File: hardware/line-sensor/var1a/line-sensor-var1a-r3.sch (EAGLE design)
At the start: 142 parts, among them IC1 GP2S60, IC10 GP2S60, IC11 GP2S60, IC12 GP2S60, IC13 GP2S60, IC14 GP2S60, IC15 GP2S60, IC16 GP2S60, IC17 GP2S60, IC18 GP2S60, IC19 GP2S60, IC2 GP2S60, IC20 GP2S60, IC21 GP2S60, IC22 GP2S60, IC23 GP2S60, IC24 GP2S60, IC25 GP2S60, IC26 GP2S60, IC27 GP2S60, IC28 STM32L151VE, IC3 GP2S60, IC32 LM5165YDRCR, IC4 GP2S60, IC5 GP2S60, IC6 GP2S60, IC7 GP2S60, IC8 GP2S60, IC9 GP2S60, J1 MOLEX-502382-06XX, J2 MOLEX-53261-0771, J3 MOLEX-502382-03XX, Y1 CRYSTALKYOCERA-CX3225GB24000D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, Y2 CRYSTALNDK-NX3215SA

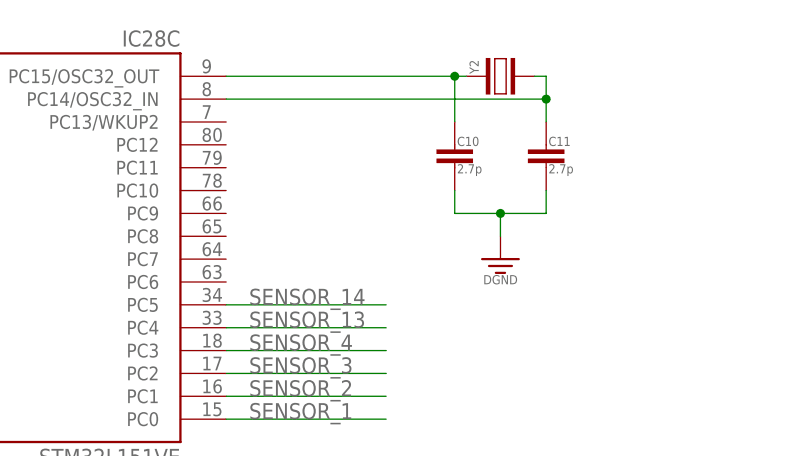
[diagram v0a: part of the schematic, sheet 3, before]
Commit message: - watchdog will now reset if either ADC or SPI didn't report in
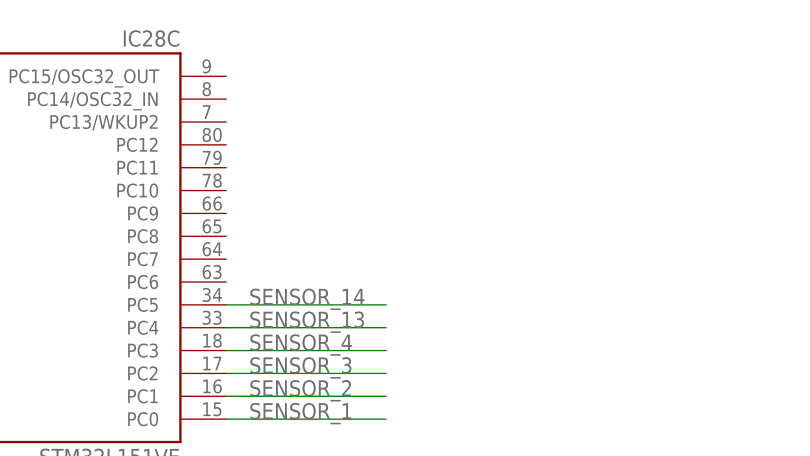
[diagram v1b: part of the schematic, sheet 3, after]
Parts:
- removed C10, C11: 2.7p, passives:CAPACITOR0402
- removed Y2: CRYSTALNDK-NX3215SA, passives:CRYSTALNDK-NX3215SA
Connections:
- removed net N$36: C10.1, IC28C.PC15/OSC32_OUT, Y2.1
- removed net N$37: C11.1, IC28C.PC14/OSC32_IN, Y2.2
- net GND: no longer C10.2, C11.2
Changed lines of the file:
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@@
 <part name="R67" library="passives" library_urn="urn:adsk.eagle:library:9287022" deviceset="RESISTOR" device="0603" package3d_urn="urn:adsk.eagle:package:704947/4" value="121k 1%"/>
 <part name="GND12" library="voltage-ground" library_urn="urn:adsk.eagle:library:704746" deviceset="GND" device=""/>
-<part name="L1" library="passives" library_urn="urn:adsk.eagle:library:9287022" deviceset="INDUCTOR" device="PANASONIC-SERIES-H" package3d_urn="urn:adsk.eagle:package:9314563/2" value="150u 0.86R 0.35A"/>
+<part name="L1" library="passives" library_urn="urn:adsk.eagle:library:9287022" deviceset="INDUCTOR" device="PANASONIC-SERIES-H" package3d_urn="urn:adsk.eagle:package:9314563/3" value="150u 0.86R 0.35A"/>
 <part name="C19" library="passives" library_urn="urn:adsk.eagle:library:9287022" deviceset="CAPACITOR" device="0603" package3d_urn="urn:adsk.eagle:package:704999/4" value="33n 10V X7R"/>
 <part name="DGND12" library="voltage-ground" library_urn="urn:adsk.eagle:library:704746" deviceset="DGND" device=""/>
 <part name="DGND13" library="voltage-ground" library_urn="urn:adsk.eagle:library:704746" deviceset="DGND" device=""/>
 <part name="R68" library="passives" library_urn="urn:adsk.eagle:library:9287022" deviceset="RESISTOR" device="0603" package3d_urn="urn:adsk.eagle:package:704947/4" value="0.5 5%"/>
-<part name="C20" library="passives" library_urn="urn:adsk.eagle:library:9287022" deviceset="CAPACITOR" device="0805" package3d_urn="urn:adsk.eagle:package:704997/4" value="22u 10V X7S"/>
+<part name="C20" library="passives" library_urn="urn:adsk.eagle:library:9287022" deviceset="CAPACITOR" device="0805" package3d_urn="urn:adsk.eagle:package:704997/5" value="22u 10V X7S"/>
 <part name="DGND14" library="voltage-ground" library_urn="urn:adsk.eagle:library:704746" deviceset="DGND" device=""/>
 <part name="SUPPLY37" library="voltage-ground" library_urn="urn:adsk.eagle:library:704746" deviceset="+3.3V" device=""/>
 <part name="FRAME5" library="frames" library_urn="urn:adsk.eagle:library:229" deviceset="A4L-LOC" device=""/>
-<part name="Y1" library="passives" library_urn="urn:adsk.eagle:library:9287022" deviceset="CRYSTAL" device="KYOCERA-CX3225GB24000D0HEQ" package3d_urn="urn:adsk.eagle:package:9990572/4"/>
+<part name="Y1" library="passives" library_urn="urn:adsk.eagle:library:9287022" deviceset="CRYSTAL" device="KYOCERA-CX3225GB24000D0HEQ" package3d_urn="urn:adsk.eagle:package:9990572/5"/>
 <part name="C8" library="passives" library_urn="urn:adsk.eagle:library:9287022" deviceset="CAPACITOR" device="0402" package3d_urn="urn:adsk.eagle:package:11874712/3" value="4.3p"/>
 <part name="C9" library="passives" library_urn="urn:adsk.eagle:library:9287022" deviceset="CAPACITOR" device="0402" package3d_urn="urn:adsk.eagle:package:11874712/3" value="4.3p"/>
 <part name="DGND15" library="voltage-ground" library_urn="urn:adsk.eagle:library:704746" deviceset="DGND" device=""/>
-<part name="Y2" library="passives" library_urn="urn:adsk.eagle:library:9287022" deviceset="CRYSTAL" device="NDK-NX3215SA" package3d_urn="urn:adsk.eagle:package:11610117/4"/>
-<part name="C10" library="passives" library_urn="urn:adsk.eagle:library:9287022" deviceset="CAPACITOR" device="0402" package3d_urn="urn:adsk.eagle:package:11874712/3" value="2.7p"/>
-<part name="C11" library="passives" library_urn="urn:adsk.eagle:library:9287022" deviceset="CAPACITOR" device="0402" package3d_urn="urn:adsk.eagle:package:11874712/3" value="2.7p"/>
-<part name="DGND16" library="voltage-ground" library_urn="urn:adsk.eagle:library:704746" deviceset="DGND" device=""/>
 <part name="C12" library="passives" library_urn="urn:adsk.eagle:library:9287022" deviceset="CAPACITOR" device="0603" package3d_urn="urn:adsk.eagle:package:704999/4" value="1u 16V X7R"/>
 <part name="GND2" library="voltage-ground" library_urn="urn:adsk.eagle:library:704746" deviceset="GND" device=""/>
@@
 <attribute name="VALUE" x="182.88" y="137.922" size="1.016" layer="96" align="top-center"/>
 </instance>
-<instance part="Y2" gate="G$1" x="121.92" y="167.64" smashed="yes" rot="R90">
-<attribute name="NAME" x="119.507" y="167.894" size="1.016" layer="95" font="vector" rot="R90"/>
-</instance>
-<instance part="C10" gate="G$1" x="116.84" y="157.48" smashed="yes">
-<attribute name="NAME" x="117.094" y="159.893" size="1.016" layer="95" font="vector"/>
-<attribute name="VALUE" x="117.094" y="156.845" size="1.016" layer="96" font="vector"/>
-</instance>
-<instance part="C11" gate="G$1" x="127" y="157.48" smashed="yes">
-<attribute name="NAME" x="127.254" y="159.893" size="1.016" layer="95" font="vector"/>
-<attribute name="VALUE" x="127.254" y="156.845" size="1.016" layer="96" font="vector"/>
-</instance>
-<instance part="DGND16" gate="G$2" x="121.92" y="147.32" smashed="yes">
-<attribute name="VALUE" x="121.92" y="145.542" size="1.016" layer="96" align="top-center"/>
-</instance>
 </instances>
 <busses>
@@
 <wire x1="180.34" y1="165.1" x2="182.88" y2="165.1" width="0.1524" layer="91"/>
 </segment>
-<segment>
-<pinref part="C10" gate="G$1" pin="2"/>
-<wire x1="116.84" y1="154.94" x2="116.84" y2="152.4" width="0.1524" layer="91"/>
-<wire x1="116.84" y1="152.4" x2="121.92" y2="152.4" width="0.1524" layer="91"/>
-<pinref part="C11" gate="G$1" pin="2"/>
-<wire x1="121.92" y1="152.4" x2="127" y2="152.4" width="0.1524" layer="91"/>
-<wire x1="127" y1="152.4" x2="127" y2="154.94" width="0.1524" layer="91"/>
-<junction x="121.92" y="152.4"/>
-<pinref part="DGND16" gate="G$2" pin="DGND"/>
-<wire x1="121.92" y1="152.4" x2="121.92" y2="149.86" width="0.1524" layer="91"/>
-</segment>
 </net>
 <net name="!RST" class="0">
@@
 </segment>
 </net>
-<net name="N$36" class="0">
-<segment>
-<pinref part="IC28" gate="C" pin="PC15/OSC32_OUT"/>
-<pinref part="Y2" gate="G$1" pin="1"/>
-<wire x1="91.44" y1="167.64" x2="116.84" y2="167.64" width="0.1524" layer="91"/>
-<junction x="116.84" y="167.64"/>
-<wire x1="116.84" y1="167.64" x2="118.11" y2="167.64" width="0.1524" layer="91"/>
-<pinref part="C10" gate="G$1" pin="1"/>
-<wire x1="116.84" y1="167.64" x2="116.84" y2="162.56" width="0.1524" layer="91"/>
-</segment>
-</net>
-<net name="N$37" class="0">
-<segment>
-<pinref part="Y2" gate="G$1" pin="2"/>
-<wire x1="125.73" y1="167.64" x2="127" y2="167.64" width="0.1524" layer="91"/>
-<wire x1="127" y1="167.64" x2="127" y2="165.1" width="0.1524" layer="91"/>
-<pinref part="IC28" gate="C" pin="PC14/OSC32_IN"/>
-<wire x1="127" y1="165.1" x2="91.44" y2="165.1" width="0.1524" layer="91"/>
-<junction x="127" y="165.1"/>
-<pinref part="C11" gate="G$1" pin="1"/>
-<wire x1="127" y1="165.1" x2="127" y2="162.56" width="0.1524" layer="91"/>
-</segment>
-</net>

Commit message: - removed 32.7 kHz crystal - replaced 24 MHz crystal with 8 MHz one - fixed ring around crustal - removed all but ground layers underneath crystal location
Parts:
- C8, C9: device passives:CAPACITOR0402 -> passives:CAPACITOR0603
- Y1: value CRYSTALKYOCERA-CX3225GB24000D0HEQ -> CRYSTALKYOCERA-CX5032GA; device passives:CRYSTALKYOCERA-CX3225GB24000D0HEQ -> passives:CRYSTALKYOCERA-CX5032GA
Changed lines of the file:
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@@
 <grid distance="0.1" unitdist="inch" unit="inch" style="lines" multiple="1" display="no" altdistance="0.01" altunitdist="inch" altunit="inch"/>
 <layers>
-<layer number="1" name="Top" color="4" fill="1" visible="no" active="no"/>
-<layer number="2" name="Route2" color="16" fill="1" visible="no" active="no"/>
-<layer number="15" name="Route15" color="23" fill="1" visible="no" active="no"/>
-<layer number="16" name="Bottom" color="1" fill="1" visible="no" active="no"/>
-<layer number="17" name="Pads" color="2" fill="1" visible="no" active="no"/>
-<layer number="18" name="Vias" color="2" fill="1" visible="no" active="no"/>
-<layer number="19" name="Unrouted" color="6" fill="1" visible="no" active="no"/>
-<layer number="20" name="Dimension" color="24" fill="1" visible="no" active="no"/>
-<layer number="21" name="tPlace" color="7" fill="1" visible="no" active="no"/>
-<layer number="22" name="bPlace" color="7" fill="1" visible="no" active="no"/>
-<layer number="23" name="tOrigins" color="15" fill="1" visible="no" active="no"/>
-<layer number="24" name="bOrigins" color="15" fill="1" visible="no" active="no"/>
-<layer number="25" name="tNames" color="7" fill="1" visible="no" active="no"/>
-<layer number="26" name="bNames" color="7" fill="1" visible="no" active="no"/>
-<layer number="27" name="tValues" color="7" fill="1" visible="no" active="no"/>
-<layer number="28" name="bValues" color="7" fill="1" visible="no" active="no"/>
+<layer number="1" name="Top" color="4" fill="1" visible="yes" active="no"/>
+<layer number="2" name="Route2" color="16" fill="1" visible="yes" active="no"/>
+<layer number="15" name="Route15" color="23" fill="1" visible="yes" active="no"/>
+<layer number="16" name="Bottom" color="1" fill="1" visible="yes" active="no"/>
+<layer number="17" name="Pads" color="2" fill="1" visible="yes" active="no"/>
+<layer number="18" name="Vias" color="2" fill="1" visible="yes" active="no"/>
+<layer number="19" name="Unrouted" color="6" fill="1" visible="yes" active="no"/>
+<layer number="20" name="Dimension" color="24" fill="1" visible="yes" active="no"/>
+<layer number="21" name="tPlace" color="7" fill="1" visible="yes" active="no"/>
+<layer number="22" name="bPlace" color="7" fill="1" visible="yes" active="no"/>
+<layer number="23" name="tOrigins" color="15" fill="1" visible="yes" active="no"/>
+<layer number="24" name="bOrigins" color="15" fill="1" visible="yes" active="no"/>
+<layer number="25" name="tNames" color="7" fill="1" visible="yes" active="no"/>
+<layer number="26" name="bNames" color="7" fill="1" visible="yes" active="no"/>
+<layer number="27" name="tValues" color="7" fill="1" visible="yes" active="no"/>
+<layer number="28" name="bValues" color="7" fill="1" visible="yes" active="no"/>
 <layer number="29" name="tStop" color="7" fill="3" visible="no" active="no"/>
 <layer number="30" name="bStop" color="7" fill="6" visible="no" active="no"/>
@@
 <layer number="35" name="tGlue" color="7" fill="4" visible="no" active="no"/>
 <layer number="36" name="bGlue" color="7" fill="5" visible="no" active="no"/>
-<layer number="37" name="tTest" color="7" fill="1" visible="no" active="no"/>
-<layer number="38" name="bTest" color="7" fill="1" visible="no" active="no"/>
+<layer number="37" name="tTest" color="7" fill="1" visible="yes" active="no"/>
+<layer number="38" name="bTest" color="7" fill="1" visible="yes" active="no"/>
 <layer number="39" name="tKeepout" color="4" fill="11" visible="no" active="no"/>
 <layer number="40" name="bKeepout" color="1" fill="11" visible="no" active="no"/>
@@
 <layer number="44" name="Drills" color="7" fill="1" visible="no" active="no"/>
 <layer number="45" name="Holes" color="7" fill="1" visible="no" active="no"/>
-<layer number="46" name="Milling" color="3" fill="1" visible="no" active="no"/>
-<layer number="47" name="Measures" color="7" fill="1" visible="no" active="no"/>
-<layer number="48" name="Document" color="7" fill="1" visible="no" active="no"/>
-<layer number="49" name="Reference" color="7" fill="1" visible="no" active="no"/>
-<layer number="50" name="dxf" color="7" fill="1" visible="no" active="no"/>
-<layer number="51" name="tDocu" color="7" fill="1" visible="no" active="no"/>
-<layer number="52" name="bDocu" color="7" fill="1" visible="no" active="no"/>
-<layer number="53" name="tGND_GNDA" color="7" fill="9" visible="no" active="no"/>
-<layer number="54" name="bGND_GNDA" color="1" fill="9" visible="no" active="no"/>
-<layer number="56" name="wert" color="7" fill="1" visible="no" active="no"/>
-<layer number="57" name="tCAD" color="7" fill="1" visible="no" active="no"/>
-<layer number="59" name="tCarbon" color="7" fill="1" visible="no" active="no"/>
-<layer number="60" name="bCarbon" color="7" fill="1" visible="no" active="no"/>
+<layer number="46" name="Milling" color="3" fill="1" visible="yes" active="no"/>
+<layer number="47" name="Measures" color="7" fill="1" visible="yes" active="no"/>
+<layer number="48" name="Document" color="7" fill="1" visible="yes" active="no"/>
+<layer number="49" name="Reference" color="7" fill="1" visible="yes" active="no"/>
+<layer number="50" name="dxf" color="7" fill="1" visible="yes" active="no"/>
+<layer number="51" name="tDocu" color="7" fill="1" visible="yes" active="no"/>
+<layer number="52" name="bDocu" color="7" fill="1" visible="yes" active="no"/>
+<layer number="53" name="tGND_GNDA" color="7" fill="9" visible="yes" active="no"/>
+<layer number="54" name="bGND_GNDA" color="1" fill="9" visible="yes" active="no"/>
+<layer number="56" name="wert" color="7" fill="1" visible="yes" active="no"/>
+<layer number="57" name="tCAD" color="7" fill="1" visible="yes" active="no"/>
+<layer number="59" name="tCarbon" color="7" fill="1" visible="yes" active="no"/>
+<layer number="60" name="bCarbon" color="7" fill="1" visible="yes" active="no"/>
 <layer number="88" name="SimResults" color="9" fill="1" visible="yes" active="yes"/>
 <layer number="89" name="SimProbes" color="9" fill="1" visible="yes" active="yes"/>
@@
 <part name="SUPPLY37" library="voltage-ground" library_urn="urn:adsk.eagle:library:704746" deviceset="+3.3V" device=""/>
 <part name="FRAME5" library="frames" library_urn="urn:adsk.eagle:library:229" deviceset="A4L-LOC" device=""/>
-<part name="Y1" library="passives" library_urn="urn:adsk.eagle:library:9287022" deviceset="CRYSTAL" device="KYOCERA-CX3225GB24000D0HEQ" package3d_urn="urn:adsk.eagle:package:9990572/5"/>
-<part name="C8" library="passives" library_urn="urn:adsk.eagle:library:9287022" deviceset="CAPACITOR" device="0402" package3d_urn="urn:adsk.eagle:package:11874712/3" value="4.3p"/>
-<part name="C9" library="passives" library_urn="urn:adsk.eagle:library:9287022" deviceset="CAPACITOR" device="0402" package3d_urn="urn:adsk.eagle:package:11874712/3" value="4.3p"/>
+<part name="Y1" library="passives" library_urn="urn:adsk.eagle:library:9287022" deviceset="CRYSTAL" device="KYOCERA-CX5032GA" package3d_urn="urn:adsk.eagle:package:14994043/1"/>
+<part name="C8" library="passives" library_urn="urn:adsk.eagle:library:9287022" deviceset="CAPACITOR" device="0603" package3d_urn="urn:adsk.eagle:package:704999/4" value="4.3p"/>
+<part name="C9" library="passives" library_urn="urn:adsk.eagle:library:9287022" deviceset="CAPACITOR" device="0603" package3d_urn="urn:adsk.eagle:package:704999/4" value="4.3p"/>
 <part name="DGND15" library="voltage-ground" library_urn="urn:adsk.eagle:library:704746" deviceset="DGND" device=""/>
 <part name="C12" library="passives" library_urn="urn:adsk.eagle:library:9287022" deviceset="CAPACITOR" device="0603" package3d_urn="urn:adsk.eagle:package:704999/4" value="1u 16V X7R"/>
